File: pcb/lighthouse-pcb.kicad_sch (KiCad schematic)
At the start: 44 parts, among them J1 USB_C_Receptacle_USB2.0, SW1 BOOT, SW2 RESET, SW3 ROOF BUTTON, SW4 SW_DIP_x06, U1 ESP32-C3-WROOM-02, U2 CN5711, U3 AP2112K-3.3

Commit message: Layout and two button design
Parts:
- removed TP4: TX, TestPoint:TestPoint_Pad_D1.0mm, symbol Connector:TestPoint_Small
- added C10: 220nf, Capacitor_SMD:C_0603_1608Metric, symbol Device:C_Small
- added D11, D12, D13, D2: WS2812B, LED_SMD:LED_WS2812B_PLCC4_5.0x5.0mm_P3.2mm, symbol LED:WS2812B
- added U4: USBLC6-2SC6, Package_TO_SOT_SMD:SOT-23-6, symbol Power_Protection:USBLC6-2SC6
- D1, R4: now left out of the parts list
- D10, D7, D8, D9: footprint LED_SMD:LED_PLCC_2835 -> lighthouse_footprints:LED_PLCC_2835; symbol Device:LED -> lighthouse_symbols:LED 0.5W
- D3: LCSC Part # (none) -> C2874885
- J1: footprint Connector_USB:USB_C_Receptacle_HRO_TYPE-C-31-M-12 -> lighthouse_footprints:USB_C_Receptacle_HRO_TYPE-C-31-M-12
- SW1: footprint Button_Switch_SMD:SW_SPST_PTS810 -> lighthouse_footprints:SW_SPST_PTS810
- SW2: footprint Button_Switch_SMD:SW_SPST_PTS810 -> lighthouse_footprints:SW_SPST_PTS810; now left out of the parts list
- SW3: value ROOF BUTTON -> ROOF; footprint Button_Switch_SMD:SW_SPST_PTS810 -> lighthouse_footprints:SW_SPST_PTS810
- SW4: value SW_DIP_x06 -> SW_DIP_x08; footprint Button_Switch_SMD:SW_DIP_SPSTx06_Slide_Copal_CHS-06A_W5.08mm_P1.27mm_JPin -> Button_Switch_SMD:SW_DIP_SPSTx08_Slide_Copal_CHS-08A_W5.08mm_P1.27mm_JPin; symbol Switch:SW_DIP_x06 -> Switch:SW_DIP_x08; LCSC Part # C3293146 -> C3293147
- TP3: value RX -> RESET; footprint TestPoint:TestPoint_Pad_D1.0mm -> lighthouse_footprints:TestPoint_Pad_D1.0mm_no_court
- U1: footprint RF_Module:ESP32-C3-WROOM-02 -> lighthouse_footprints:ESP32-C3-WROOM-02
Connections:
- net +3.3V is gone; now on net +3V3: C2.1, C3.1, C6.1, R1.1, R2.1, R3.2, TP2.1, U1.1 (3V3), U3.5 (VOUT)
- net +5V: now also D3.1 (VDD), D4.1 (VDD), D5.1 (VDD), D6.1 (VDD), C10.1, D11.1 (VDD), D12.1 (VDD), D13.1 (VDD), D2.1 (VDD), U4.5 (VBUS)
- net GND: now also D3.3 (VSS), D4.3 (VSS), D5.3 (VSS), D6.3 (VSS), SW4.13, SW4.14, SW4.15, SW4.16, C10.2, D11.3 (VSS), D12.3 (VSS), D13.3 (VSS), D2.3 (VSS), U4.2 (GND); no longer SW4.7, SW4.8
- net GPIO0: now also SW4.4; no longer SW4.1
- net GPIO1: now also SW4.3; no longer SW4.2
- net GPIO3: now also SW4.2; no longer SW4.3
- net GPIO4: now also SW4.5; no longer SW4.4
- net GPIO5: now also SW4.6; no longer SW4.5
- net GPIO6: now also SW4.7; no longer SW4.6
- net GPIO7: now also SW4.8
- net GPIO8: no longer D3.4 (DIN)
- net RX: now also D3.4 (DIN); no longer TP3.1
- net TX: now also SW4.1
- net USB_D+: now also U4.4 (I/O2); no longer J1.A6 (D+), J1.B6 (D+)
- net USB_D-: now also U4.6 (I/O1); no longer J1.A7 (D-), J1.B7 (D-)
- net at C1.2, R2.2, SW2.2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: now also TP3.1
- net at D6.2 (DOUT): now also D2.4 (DIN)
- new net: D12.2 (DOUT), D13.4 (DIN)
- new net: D11.2 (DOUT), D12.4 (DIN)
- new net: D11.4 (DIN), D2.2 (DOUT)
- new net D+: J1.A6 (D+), J1.B6 (D+), U4.3 (I/O2)
- new net D-: J1.A7 (D-), J1.B7 (D-), U4.1 (I/O1)
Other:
- note added: "Excluded"
- moved on the sheet: D3, D4, D5, D6, R5, R6

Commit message: REV A release
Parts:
- added H4: MountingHole M2.5, lighthouse_footprints:MountingHole_2.7mm_M2.5, symbol Mechanical:MountingHole
- added R12, R13: 10k, Resistor_SMD:R_0603_1608Metric, symbol Device:R_Small
- added TP4: IO8, TestPoint:TestPoint_Pad_D1.0mm, symbol Connector:TestPoint_Small
- added TP5: GND, TestPoint:TestPoint_Pad_D1.0mm, symbol Connector:TestPoint_Small
- added TP6: 5V, TestPoint:TestPoint_Pad_D1.0mm, symbol Connector:TestPoint_Small
- C2, H1, H2, H3: now left out of the parts list
- D11, D12, D13, D2, D4, D5, D6: LCSC Part # (none) -> C2874885
- SW1: value BOOT -> BOOT/ROOF; footprint lighthouse_footprints:SW_SPST_PTS810 -> lighthouse_footprints:SW_Push_1P1T_XKB_TS-1187A; LCSC Part # C139797 -> C318885
- SW3: value ROOF -> FRONT; footprint lighthouse_footprints:SW_SPST_PTS810 -> lighthouse_footprints:SW_Push_1P1T-MP_NO_Horizontal_Alps_SKRTLAE010; LCSC Part # C139797 -> C561509
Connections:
- net +5V: now also TP6.1
- net GND: now also SW3.1, SW3.MP (Shield), R12.2, R13.2, TP5.1; no longer SW3.2
- net GPIO0: now also D3.4 (DIN), R12.1; no longer SW4.4
- net GPIO1: now also U2.8 (CE), R13.1; no longer SW4.3
- net GPIO10: now also SW4.1; no longer SW3.1
- net GPIO2: now also SW3.2; no longer U2.8 (CE)
- net GPIO3: now also SW4.4; no longer SW4.2
- net GPIO8: now also TP4.1
- net EN: now reaches C1.2, R2.2, SW2.2, TP3.1, U1.2 (EN)
- net RX renamed RX/20
- net RX/20: now also SW4.2; no longer D3.4 (DIN)
- net TX renamed TX/21
- net TX/21: now also SW4.3; no longer SW4.1

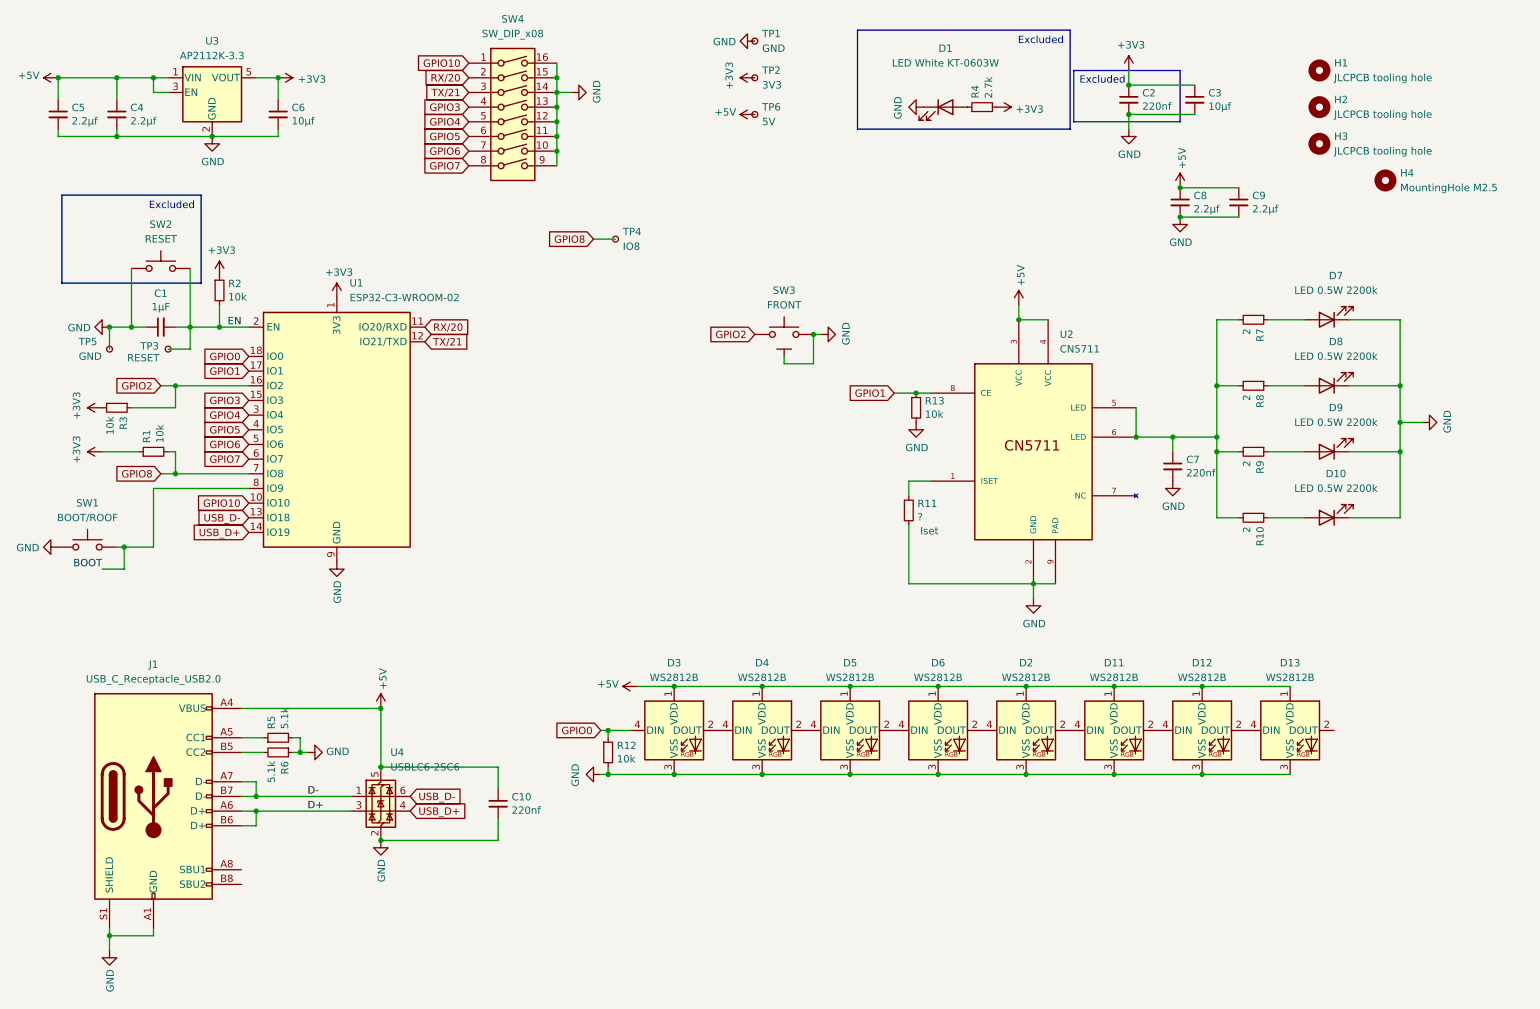
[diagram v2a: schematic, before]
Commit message: Update GPIO0-2 schematic and layout
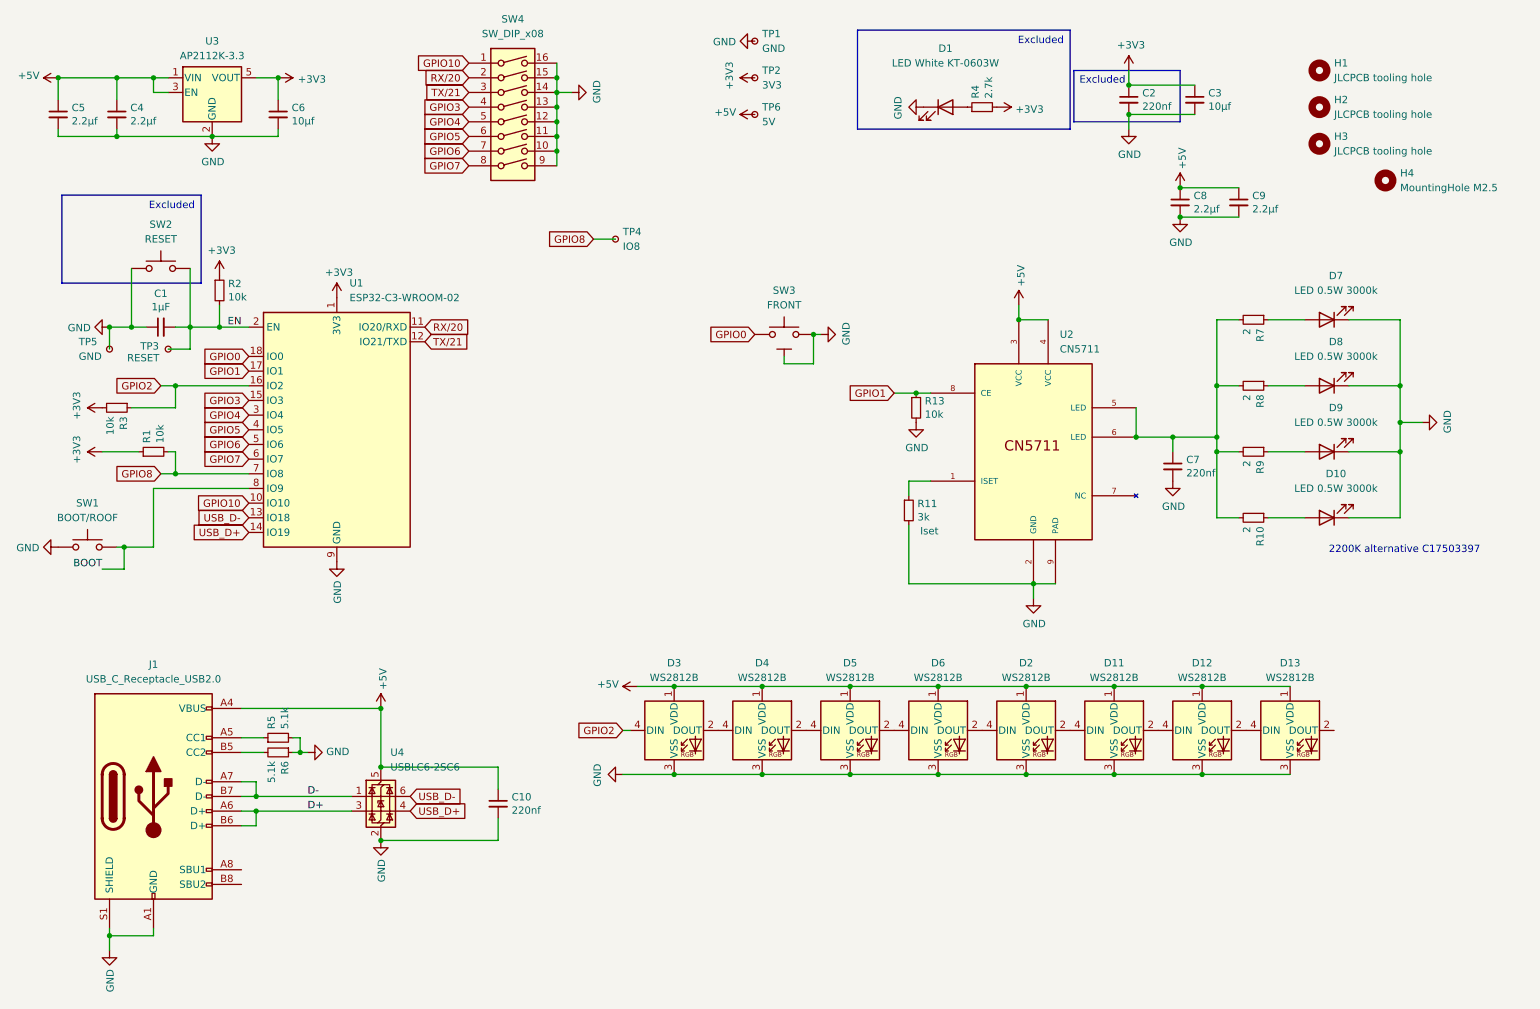
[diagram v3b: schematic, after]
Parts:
- removed R12: 10k, Resistor_SMD:R_0603_1608Metric, symbol Device:R_Small
- D10, D7, D8, D9: value LED 0.5W 2200k -> LED 0.5W 3000k; LCSC Part # C17503397 -> C694723
- R11: value ? -> 3k; LCSC Part # (none) -> C4211
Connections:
- net GPIO0: now also SW3.2; no longer D3.4 (DIN)
- net GPIO2: now also D3.4 (DIN); no longer SW3.2
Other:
- note added: "2200K alternative C17503397"
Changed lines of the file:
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@@
 	)
 	(junction
-		(at 127 149.86)
-		(diameter 0)
-		(color 0 0 0 0)
-	)
-	(junction
 		(at 198.12 71.12)
 		(diameter 0)
@@
 	)
 	(junction
-		(at 127 142.24)
-		(diameter 0)
-		(color 0 0 0 0)
-	)
-	(junction
 		(at 229.87 134.62)
 		(diameter 0)
@@
 	(wire
 		(pts
-			(xy 125.73 149.86) (xy 127 149.86)
+			(xy 129.54 149.86) (xy 138.43 149.86)
 		)
 		(stroke
@@
 	(wire
 		(pts
-			(xy 127 149.86) (xy 138.43 149.86)
-		)
-		(stroke
-			(width 0)
-			(type default)
-		)
-	)
-	(wire
-		(pts
 			(xy 40.64 176.53) (xy 40.64 177.8)
 		)
@@
 	(wire
 		(pts
-			(xy 127 142.24) (xy 127 143.51)
-		)
-		(stroke
-			(width 0)
-			(type default)
-		)
-	)
-	(wire
-		(pts
 			(xy 118.11 36.83) (xy 118.11 39.37)
 		)
@@
 	(wire
 		(pts
-			(xy 127 148.59) (xy 127 149.86)
-		)
-		(stroke
-			(width 0)
-			(type default)
-		)
-	)
-	(wire
-		(pts
 			(xy 200.66 116.84) (xy 204.47 116.84)
 		)
@@
 	(wire
 		(pts
-			(xy 127 142.24) (xy 130.81 142.24)
-		)
-		(stroke
-			(width 0)
-			(type default)
-		)
-	)
-	(wire
-		(pts
 			(xy 66.04 156.21) (xy 66.04 158.75)
 		)
@@
 	(wire
 		(pts
-			(xy 125.73 142.24) (xy 127 142.24)
+			(xy 129.54 142.24) (xy 130.81 142.24)
 		)
 		(stroke
@@
 		)
 	)
+	(text "2200K alternative C17503397"
+		(exclude_from_sim no)
+		(at 264.922 110.998 0)
+		(effects
+			(font
+				(size 1.27 1.27)
+			)
+		)
+	)
 	(text "Excluded"
 		(exclude_from_sim no)
@@
 	(global_label "GPIO0"
 		(shape input)
-		(at 125.73 142.24 180)
+		(at 152.4 73.66 180)
 		(fields_autoplaced yes)
 		(effects
@@
 		)
 		(property "Intersheetrefs" "${INTERSHEET_REFS}"
-			(at 117.06 142.24 0)
+			(at 143.73 73.66 0)
 			(effects
 				(font
@@
 	(global_label "GPIO2"
 		(shape input)
-		(at 152.4 73.66 180)
+		(at 129.54 142.24 180)
 		(fields_autoplaced yes)
 		(effects
@@
 		)
 		(property "Intersheetrefs" "${INTERSHEET_REFS}"
-			(at 143.73 73.66 0)
+			(at 120.87 142.24 0)
 			(effects
 				(font
@@
 			)
 		)
-		(property "Value" "LED 0.5W 2200k"
+		(property "Value" "LED 0.5W 3000k"
 			(at 253.0475 88.9 0)
 			(effects
@@
 			)
 		)
-		(property "LCSC Part #" "C17503397"
+		(property "LCSC Part #" "C694723"
 			(at 251.46 93.98 0)
 			(effects
@@
 			)
 		)
-		(property "Value" "LED 0.5W 2200k"
+		(property "Value" "LED 0.5W 3000k"
 			(at 253.0475 66.04 0)
 			(effects
@@
 			)
 		)
-		(property "LCSC Part #" "C17503397"
+		(property "LCSC Part #" "C694723"
 			(at 251.46 71.12 0)
 			(effects
@@
 	(symbol
 		(lib_id "power:GND")
-		(at 125.73 149.86 270)
+		(at 129.54 149.86 270)
 		(unit 1)
 		(exclude_from_sim no)
@@
 		(dnp no)
 		(property "Reference" "#PWR016"
-			(at 119.38 149.86 0)
+			(at 123.19 149.86 0)
 			(effects
 				(font
@@
 		)
 		(property "Value" "GND"
-			(at 121.3358 149.987 0)
+			(at 125.1458 149.987 0)
 			(effects
 				(font
@@
 		)
 		(property "Footprint" ""
-			(at 125.73 149.86 0)
+			(at 129.54 149.86 0)
 			(effects
 				(font
@@
 		)
 		(property "Datasheet" ""
-			(at 125.73 149.86 0)
+			(at 129.54 149.86 0)
 			(effects
 				(font
@@
 		)
 		(property "Description" ""
-			(at 125.73 149.86 0)
+			(at 129.54 149.86 0)
 			(effects
 				(font
@@
 			)
 		)
-		(property "Value" "?"
+		(property "Value" "3k"
 			(at 180.5686 105.283 0)
 			(effects
@@
 			)
 		)
-		(property "LCSC Part #" ""
+		(property "LCSC Part #" "C4211"
 			(at 179.07 104.14 0)
 			(effects
@@
 	)
 	(symbol
-		(lib_id "Device:R_Small")
-		(at 127 146.05 0)
-		(unit 1)
-		(exclude_from_sim no)
-		(in_bom yes)
-		(on_board yes)
-		(dnp no)
-		(property "Reference" "R12"
-			(at 128.4986 144.8816 0)
-			(effects
-				(font
-					(size 1.27 1.27)
-				)
-				(justify left)
-			)
-		)
-		(property "Value" "10k"
-			(at 128.4986 147.193 0)
-			(effects
-				(font
-					(size 1.27 1.27)
-				)
-				(justify left)
-			)
-		)
-		(property "Footprint" "Resistor_SMD:R_0603_1608Metric"
-			(at 127 146.05 0)
-			(effects
-				(font
-					(size 1.27 1.27)
-				)
-				(hide yes)
-			)
-		)
-		(property "Datasheet" "~"
-			(at 127 146.05 0)
-			(effects
-				(font
-					(size 1.27 1.27)
-				)
-				(hide yes)
-			)
-		)
-		(property "Description" ""
-			(at 127 146.05 0)
-			(effects
-				(font
-					(size 1.27 1.27)
-				)
-				(hide yes)
-			)
-		)
-		(property "LCSC Part #" "C25804"
-			(at 127 146.05 0)
-			(effects
-				(font
-					(size 1.27 1.27)
-				)
-				(hide yes)
-			)
-		)
-		(pin "1"
-		)
-		(pin "2"
-		)
-		(instances
-			(project "lighthouse-pcb"
-				(path "/b9b96d54-3add-4166-9e7a-45d352891d50"
-					(reference "R12")
-					(unit 1)
-				)
-			)
-		)
-	)
-	(symbol
 		(lib_id "esp32-dimmer-slim-rescue:+3.3V-power")
 		(at 217.17 27.94 0)
@@
 			)
 		)
-		(property "Value" "LED 0.5W 2200k"
+		(property "Value" "LED 0.5W 3000k"
 			(at 253.0475 77.47 0)
 			(effects
@@
 			)
 		)
-		(property "LCSC Part #" "C17503397"
+		(property "LCSC Part #" "C694723"
 			(at 251.46 82.55 0)
 			(effects
@@
 			)
 		)
-		(property "Value" "LED 0.5W 2200k"
+		(property "Value" "LED 0.5W 3000k"
 			(at 253.0475 100.33 0)
 			(effects
@@
 			)
 		)
-		(property "LCSC Part #" "C17503397"
+		(property "LCSC Part #" "C694723"
 			(at 251.46 105.41 0)
 			(effects

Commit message: Added missing JLC part numbers and fixed U3 missing trace
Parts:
- TP1, TP2, TP3, TP4, TP5, TP6: now left out of the parts list
- U1: LCSC Part # (none) -> C2934560
- U3: LCSC Part # (none) -> C51118
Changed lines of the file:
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@@
 		(unit 1)
 		(exclude_from_sim no)
-		(in_bom yes)
+		(in_bom no)
 		(on_board yes)
 		(dnp no)
@@
 		(unit 1)
 		(exclude_from_sim no)
-		(in_bom yes)
+		(in_bom no)
 		(on_board yes)
 		(dnp no)
@@
 		(unit 1)
 		(exclude_from_sim no)
-		(in_bom yes)
+		(in_bom no)
 		(on_board yes)
 		(dnp no)
@@
 		(unit 1)
 		(exclude_from_sim no)
-		(in_bom yes)
+		(in_bom no)
 		(on_board yes)
 		(dnp no)
@@
 		(unit 1)
 		(exclude_from_sim no)
-		(in_bom yes)
+		(in_bom no)
 		(on_board yes)
 		(dnp no)
@@
 		(unit 1)
 		(exclude_from_sim no)
-		(in_bom yes)
+		(in_bom no)
 		(on_board yes)
 		(dnp no)
@@
 			)
 		)
+		(property "LCSC Part #" "C2934560"
+			(at 80.01 90.17 0)
+			(effects
+				(font
+					(size 1.27 1.27)
+				)
+				(hide yes)
+			)
+		)
 		(pin "19"
 		)
@@
 			(at 58.42 31.75 0)
 			(effects
+				(font
+					(size 1.27 1.27)
+				)
+				(hide yes)
+			)
+		)
+		(property "LCSC Part #" "C51118"
+			(at 58.42 31.75 0)
+			(effects
